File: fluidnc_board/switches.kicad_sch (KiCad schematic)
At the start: 12 parts

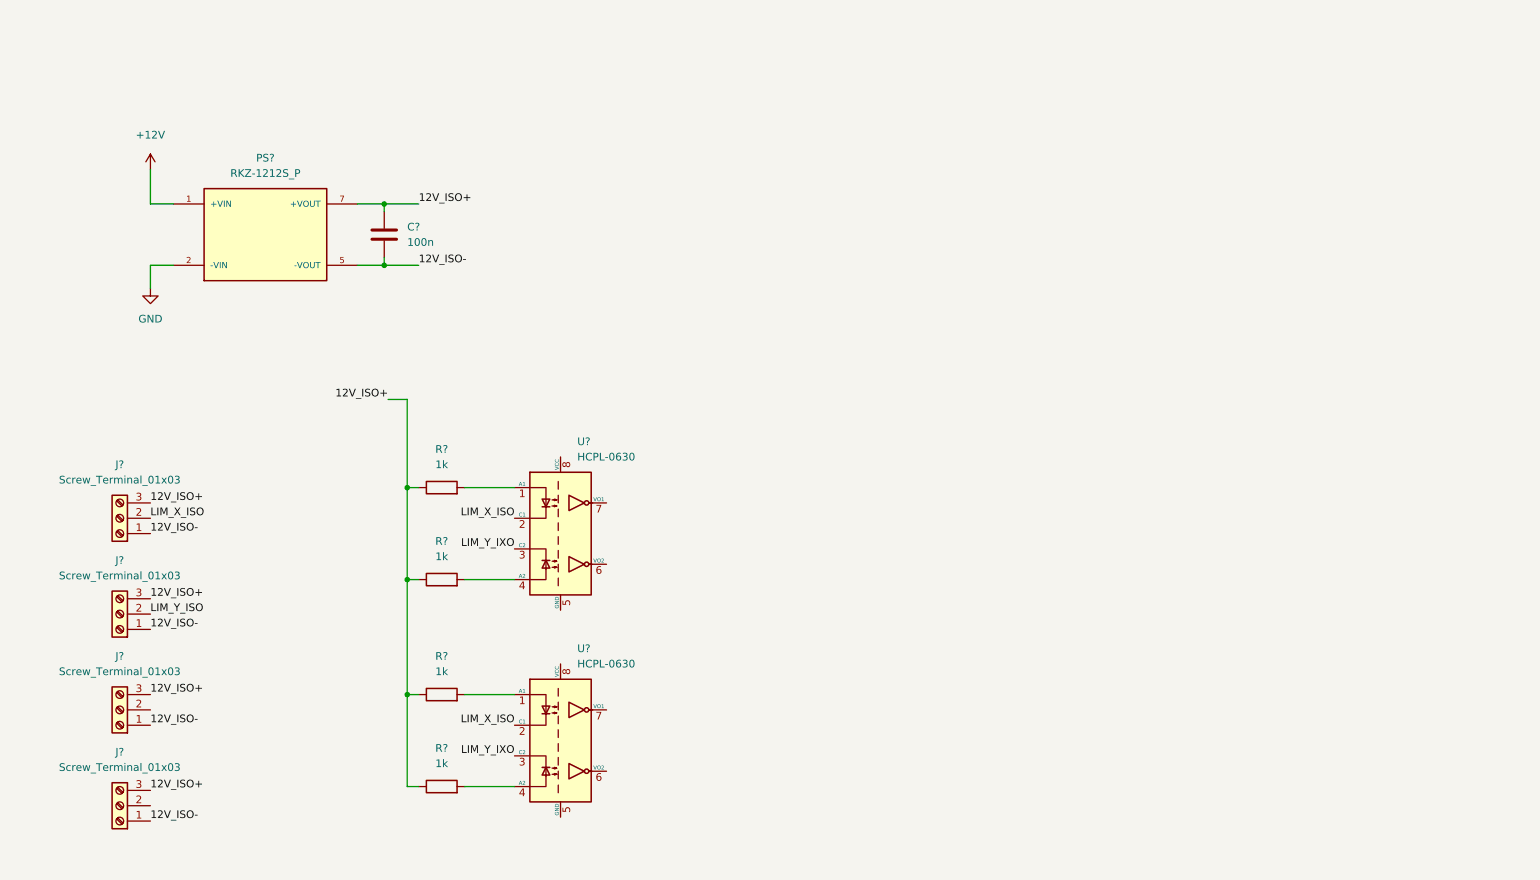
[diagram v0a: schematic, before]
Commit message: outputs, spindle output and switch inputs
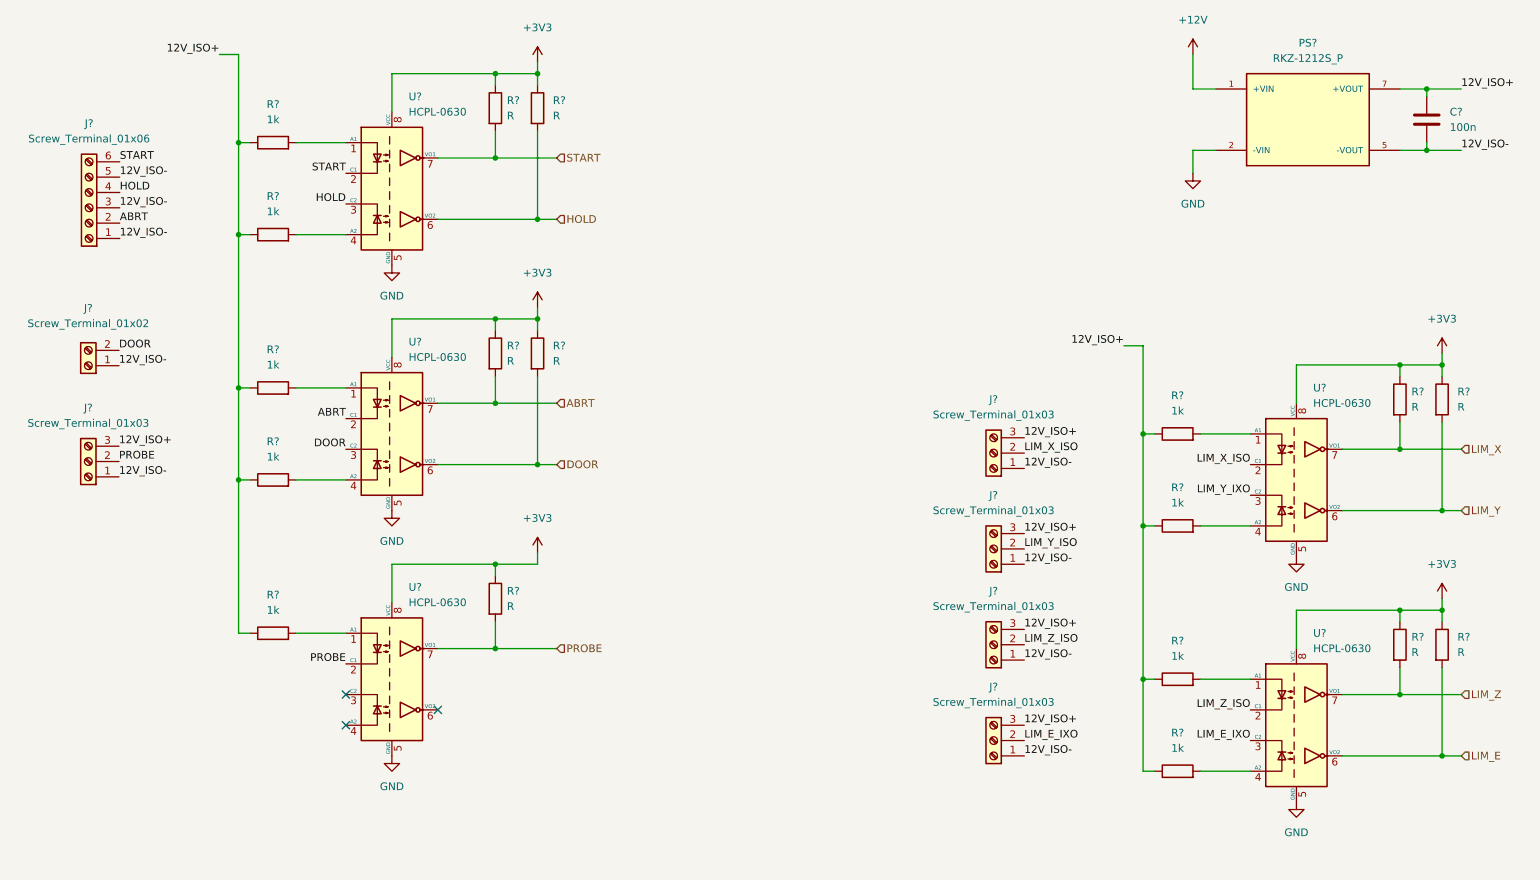
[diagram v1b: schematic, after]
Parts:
- added J?: Screw_Terminal_01x06, symbol Connector:Screw_Terminal_01x06
- added J?: Screw_Terminal_01x03, symbol Connector:Screw_Terminal_01x03
- added J?: Screw_Terminal_01x02, symbol Connector:Screw_Terminal_01x02
- added R? (x9): R, symbol Device:R
- added R? (x5): 1k, symbol Device:R
- added U? (x3): HCPL-0630, Package_SO:SOIC-8_3.9x4.9mm_P1.27mm, symbol Isolator:HCPL-0630
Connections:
- net 12V_ISO+: now also J?.3 (Pin_3), R?.1, R?.1, R?.1, R?.1, R?.1
- net 12V_ISO-: now also J?.1 (Pin_1), J?.1 (Pin_1), J?.1 (Pin_1), J?.3 (Pin_3), J?.5 (Pin_5)
- net GND: now also U?.5 (GND), U?.5 (GND), U?.5 (GND), U?.5 (GND), U?.5 (GND)
- net LIM_X_ISO: no longer U?.2 (C1)
- net LIM_Y_IXO: no longer U?.3 (C2)
- net LIM_Y: now reaches U?.6 (VO2)
- net LIM_Y: now also R?.2
- net LIM_X: now reaches U?.7 (VO1)
- net LIM_X: now also R?.2
- net +3V3: now reaches U?.8 (VCC)
- net +3V3: now also U?.8 (VCC), R?.1, R?.1, R?.1, R?.1, R?.1, R?.1, R?.1, R?.1, R?.1, U?.8 (VCC), U?.8 (VCC), U?.8 (VCC)
- net LIM_Z_ISO: now reaches J?.2 (Pin_2)
- net LIM_Z_ISO: now also U?.2 (C1)
- net LIM_E_IXO: now reaches J?.2 (Pin_2)
- net LIM_E_IXO: now also U?.3 (C2)
- net LIM_E: now reaches U?.6 (VO2)
- net LIM_E: now also R?.2
- net LIM_Z: now reaches U?.7 (VO1)
- net LIM_Z: now also R?.2
- new net: R?.2, U?.1 (A1) (x3)
- new net: R?.2, U?.4 (A2) (x2)
- new net ABRT: J?.2 (Pin_2), R?.2, U?.2 (C1), U?.7 (VO1)
- new net DOOR: J?.2 (Pin_2), R?.2, U?.3 (C2), U?.6 (VO2)
- new net HOLD: J?.4 (Pin_4), R?.2, U?.3 (C2), U?.6 (VO2)
- new net PROBE: J?.2 (Pin_2), R?.2, U?.2 (C1), U?.7 (VO1)
- new net START: J?.6 (Pin_6), R?.2, U?.2 (C1), U?.7 (VO1)
- no-connect marks 0 -> 3
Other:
- moved on the sheet: C?, J?, PS?, R?, U?

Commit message: remove unnecessary i2s chip
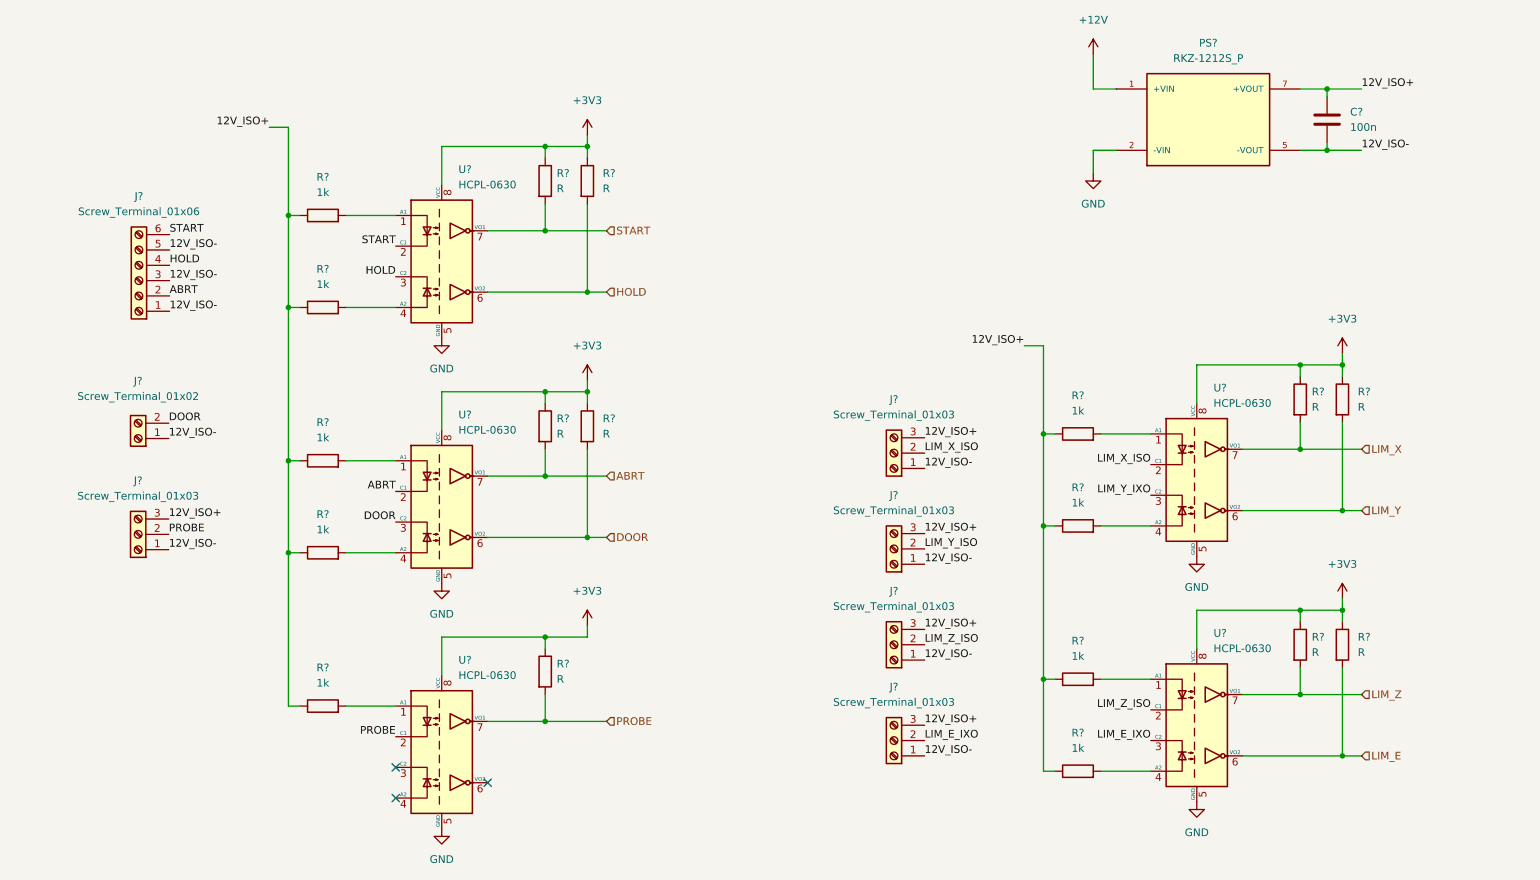
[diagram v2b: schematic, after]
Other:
- title: (none) -> Switch Inputs
- moved on the sheet: C?, J?, PS?, R?, U?

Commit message: footprint associations and part no.
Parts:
- C90: renamed from C?; footprint (none) -> Capacitor_SMD:C_0603_1608Metric_Pad1.05x0.95mm_HandSolder; Digikey Part No. (none) -> 1276-1941-1-ND
- J21: renamed from J?; footprint (none) -> Connector_Phoenix_MC:PhoenixContact_MC_1,5_2-G-3.81_1x02_P3.81mm_Horizontal
- J22, J24, J25, J26, J27: renamed from J?; footprint (none) -> Connector_Phoenix_MC:PhoenixContact_MC_1,5_3-G-3.81_1x03_P3.81mm_Horizontal
- J23: renamed from J?; footprint (none) -> Connector_Phoenix_MC:PhoenixContact_MC_1,5_6-G-3.81_1x06_P3.81mm_Horizontal
- PS2: renamed from PS?; footprint CONV_RKZ-1212S/P -> fluidnc_board:CONV_RKZ; Digikey Part No. (none) -> 945-1205-ND; MANUFACTURER RECOM -> (none); MAXIMUM_PACKAGE_HEIGHT 10.2mm -> (none); PARTREV 5 -> (none); STANDARD Manufacturer Recommendations -> (none)
- R72, R73, R74, R75, R76, R82, R83, R84, R85: renamed from R?; footprint (none) -> Resistor_SMD:R_1206_3216Metric_Pad1.30x1.75mm_HandSolder; Digikey Part No. (none) -> 311-1.00KFRCT-ND
- R77, R78, R79, R80, R81, R86, R87, R88, R89: renamed from R?; value R -> 1k; footprint (none) -> Resistor_SMD:R_1206_3216Metric_Pad1.30x1.75mm_HandSolder; Digikey Part No. (none) -> 311-1.00KFRCT-ND
- U27, U28, U29, U30, U31: renamed from U?; Digikey Part No. (none) -> 516-1487-1-ND

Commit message: fixed some footprint associations, placed footprints
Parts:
- C90: footprint Capacitor_SMD:C_0603_1608Metric_Pad1.05x0.95mm_HandSolder -> Capacitor_SMD:C_0603_1608Metric_Pad1.08x0.95mm_HandSolder; Digikey Part No. 1276-1941-1-ND -> (none)
- PS2: Digikey Part No. 945-1205-ND -> (none); MANUFACTURER (none) -> RECOM; MAXIMUM_PACKAGE_HEIGHT (none) -> 10.2mm; PARTREV (none) -> 5; STANDARD (none) -> Manufacturer Recommendations
- R72, R73, R74, R75, R76, R77, R78, R79, R80, R81, R82, R83, R84, R85, R86, R87, R88, R89: Digikey Part No. 311-1.00KFRCT-ND -> (none)
- U27, U28, U29, U30, U31: Digikey Part No. 516-1487-1-ND -> (none)

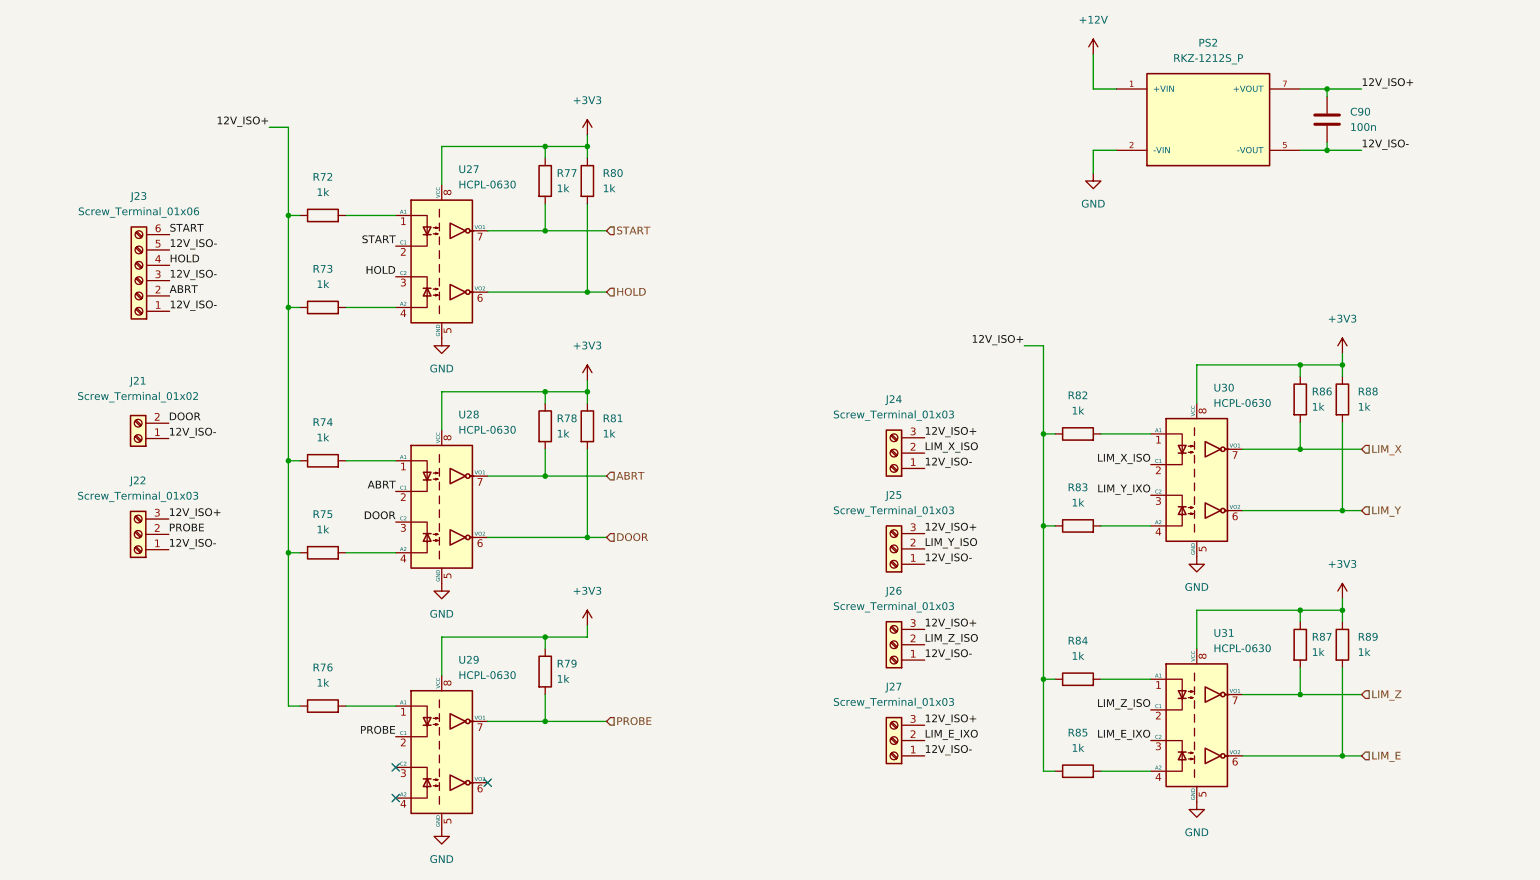
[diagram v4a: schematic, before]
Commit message: one driver unit layout
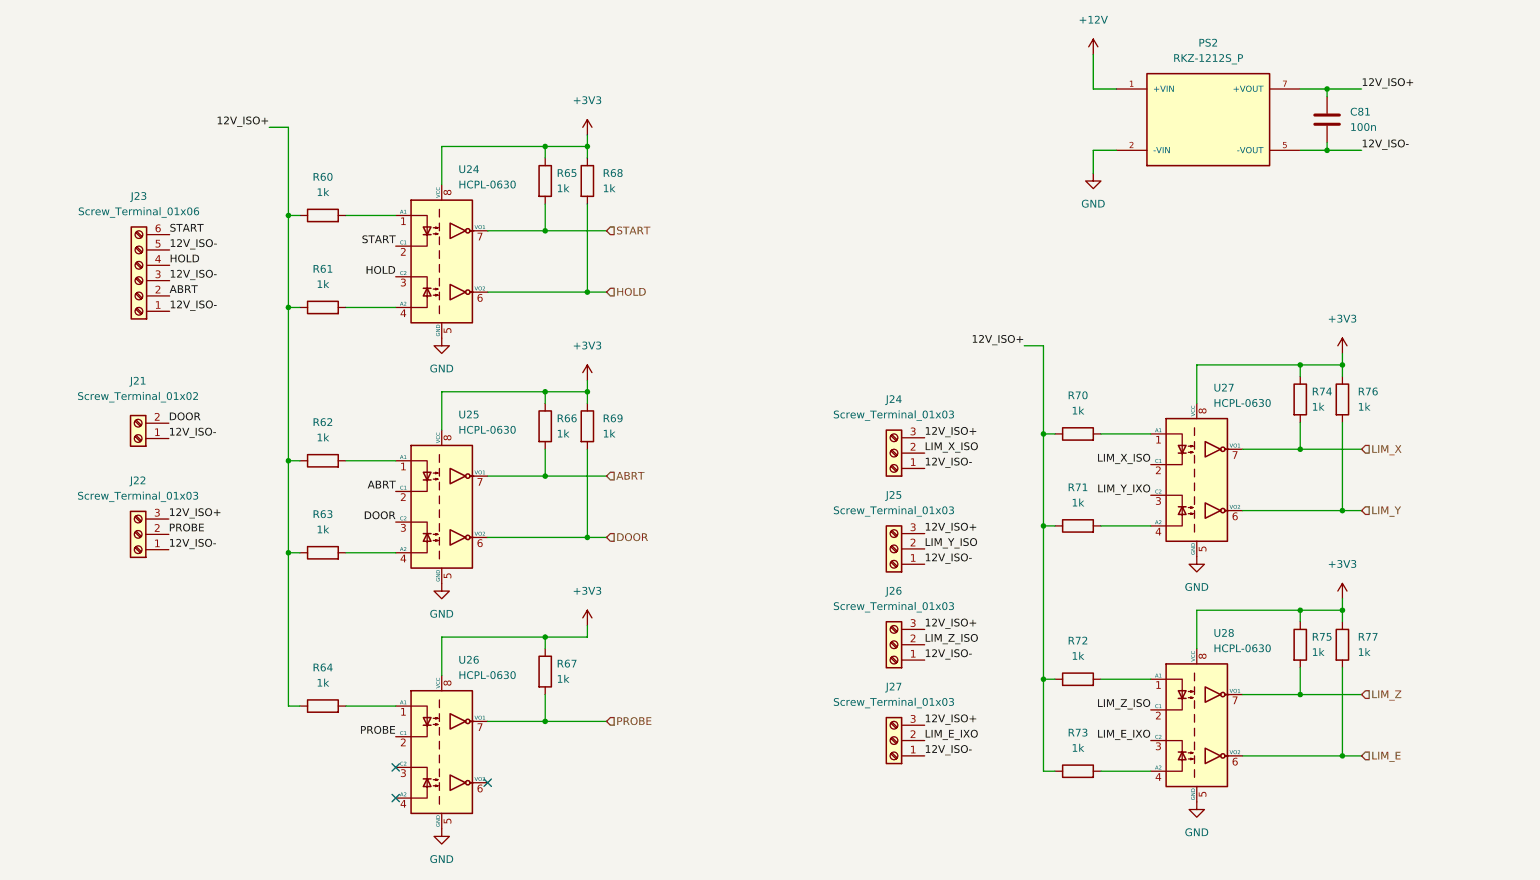
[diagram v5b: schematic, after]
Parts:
- renumbered C90 to C81, R72 to R60, R73 to R61, R74 to R62, R75 to R63, R76 to R64, R77 to R65, R78 to R66, R79 to R67, R80 to R68, R81 to R69, R82 to R70, R83 to R71, R84 to R72, R85 to R73, R86 to R74, R87 to R75, R88 to R76, R89 to R77, U27 to U24, U28 to U25, U29 to U26, U30 to U27, U31 to U28
